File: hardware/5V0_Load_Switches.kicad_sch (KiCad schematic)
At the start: 28 parts, among them Q18 SI2302DDS-T1-GE3, Q19 SI2302DDS-T1-GE3, Q20 SI2302DDS-T1-GE3, U1 LMV321RIYLT, U10 INA199C3DCKR, U4 INA199C1DCKR, U5 NVTFS5116PLTAG, U6 NVTFS5116PLTAG, U7 NVTFS5116PLTAG, U9 INA199C3DCKR

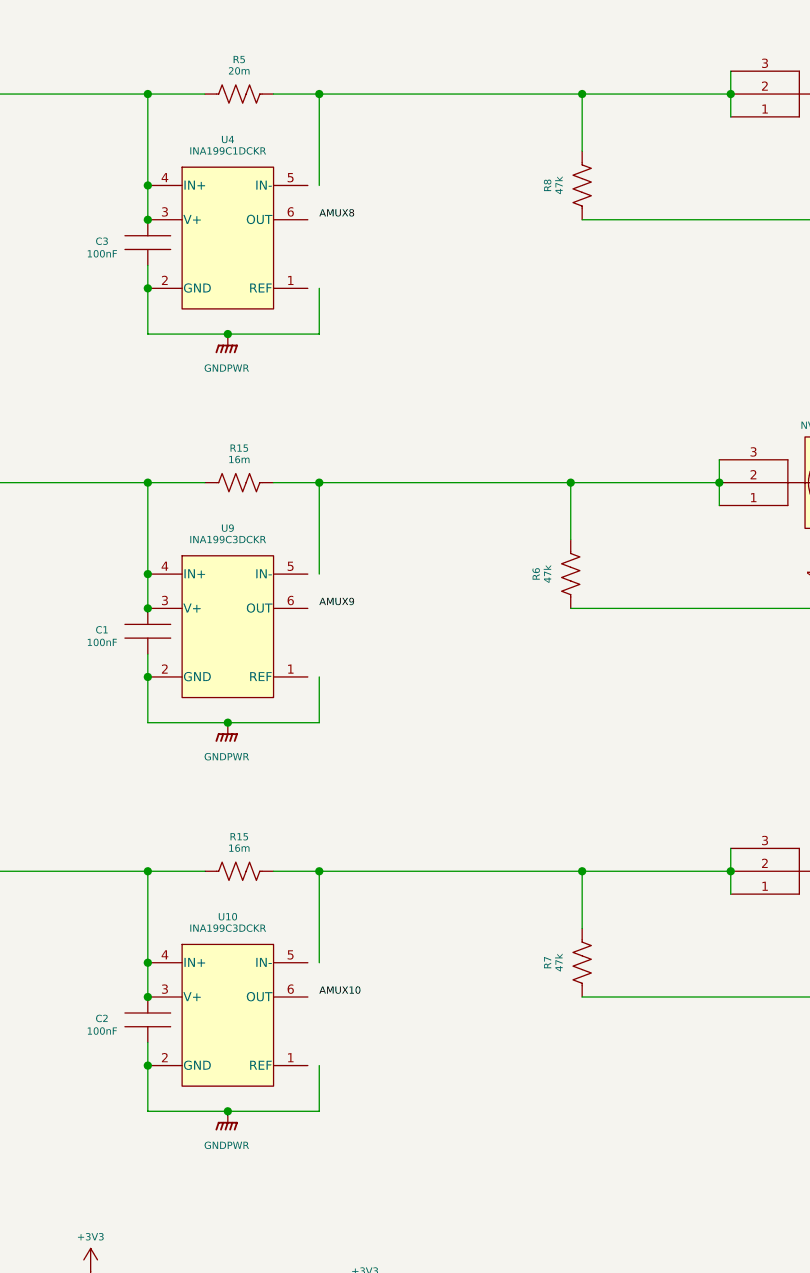
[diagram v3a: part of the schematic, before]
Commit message: hardware: Minor improvements to the schematics
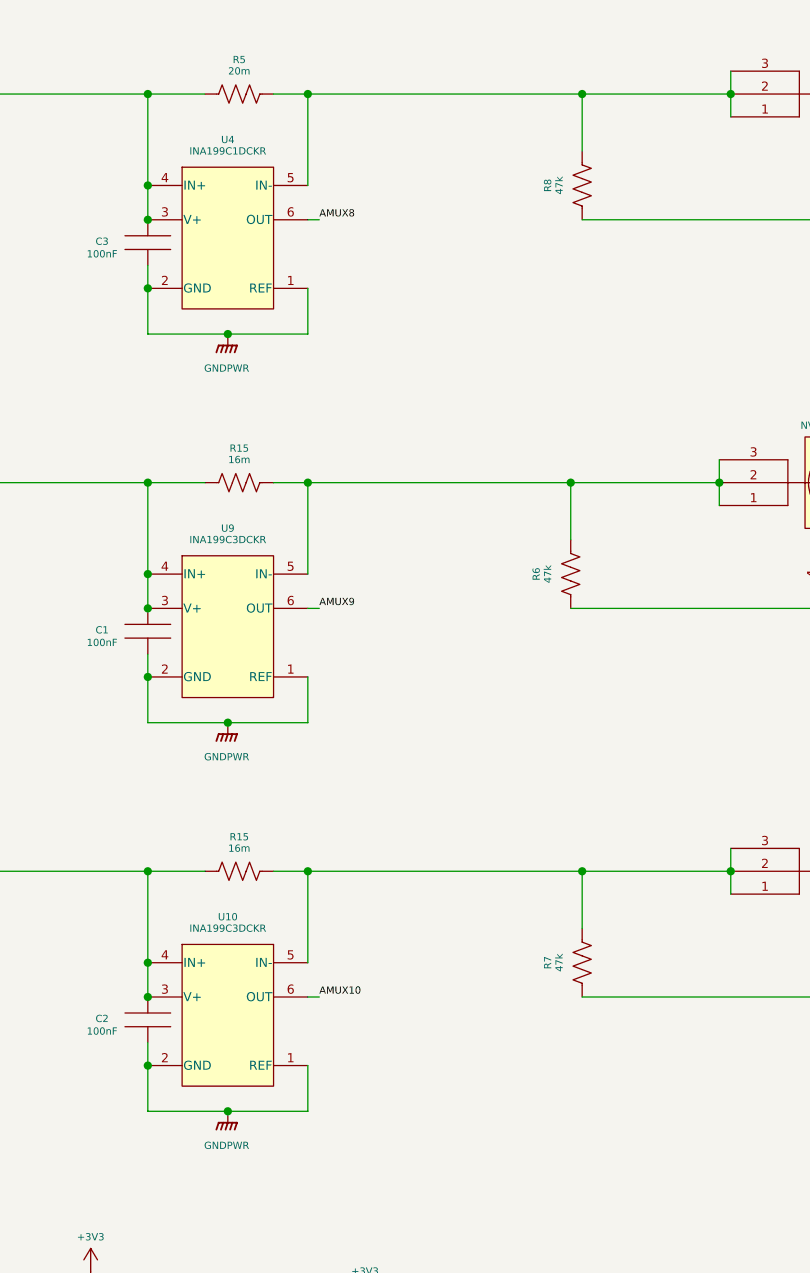
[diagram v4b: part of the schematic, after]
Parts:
- R106: MPN (none) -> CRCW060315K0FKEAHP; Manufacturer (none) -> Vishay; Package (none) -> SMD 0603; automotive Yes -> (none); automotive grade Grade 0 -> (none); category Res -> (none); composition Thick Film -> (none); device class L1 Passive Components -> (none); device class L2 Resistors -> (none); device class L3 Chip SMD Resistors -> (none); height 0.55mm -> (none); ipc land pattern name RESC16085X45 -> (none); lead free Yes -> (none); library id cdcefd0caca947c7 -> (none); manufacturer Vishay -> (none); package 0603 -> (none); power 250mW -> (none); power rating 0.33W -> (none); resistance 15kΩ -> (none); rohs Yes -> (none); series CRCW-HP e3 -> (none); temperature coefficient 100ppm/°C -> (none); temperature range high +155°C -> (none); temperature range low -55°C -> (none); tolerance 1% -> (none); voltage rating 75V -> (none)
- R2: symbol RC0805FR-0710KL:RES -> RC0805FR-0710KL:RC0805FR-0710KL; MPN (none) -> RC0805FR-0710KL; Manufacturer (none) -> YAGEO; Package (none) -> SMD 0805
- U4: footprint footprints:INA199C1DCKR -> footprints:INA199C1DCKR
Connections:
- net AMUX10: now also U10.6 (OUT)
- net AMUX8: now also U4.6 (OUT)
- net AMUX9: now also U9.6 (OUT)
- net GNDPWR: now also U10.1 (REF), U4.1 (REF), U9.1 (REF)
- net at R15.2, R7.2, U6.1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: now also U10.5 (IN-)
- net at R15.2, R6.2, U5.1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: now also U9.5 (IN-)
- net at R5.2, R8.2, U7.1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: now also U4.5 (IN-)

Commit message: hardware: Minor modifications for the upcoming release
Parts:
- R15: footprint footprints:WSL2010R0330FEA -> footprints:WSL2010R0160FEA; MPN WSL2010R0330FEA -> WSL2010R0160FEA
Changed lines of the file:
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@@
       (effects (font (size 0.8 0.8)))
     )
-    (property "Footprint" "footprints:WSL2010R0330FEA" (at 64.77 125.73 0)
+    (property "Footprint" "footprints:WSL2010R0160FEA" (at 64.77 125.73 0)
       (effects (font (size 1.27 1.27) italic) hide)
     )
@@
       (effects (font (size 1.27 1.27) italic) hide)
     )
-    (property "MPN" "WSL2010R0330FEA" (at 63.5 120.65 0)
+    (property "MPN" "WSL2010R0160FEA" (at 63.5 120.65 0)
       (effects (font (size 1.27 1.27)) hide)
     )
@@
       (effects (font (size 0.8 0.8)))
     )
-    (property "Footprint" "footprints:WSL2010R0330FEA" (at 64.77 82.55 0)
+    (property "Footprint" "footprints:WSL2010R0160FEA" (at 64.77 82.55 0)
       (effects (font (size 1.27 1.27) italic) hide)
     )
@@
       (effects (font (size 1.27 1.27) italic) hide)
     )
-    (property "MPN" "WSL2010R0330FEA" (at 63.5 77.47 0)
-      (effects (font (size 1.27 1.27)) hide)
-    )
+    (property "MPN" "WSL2010R0160FEA" (at 63.5 77.47 0)
+      (effects (font (size 1.27 1.27)) hide)
+    )

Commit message: hardware: update schematic and layout projects
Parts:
- R16: renamed from R2; Manufacturer YAGEO -> YAGEO
- U8: renamed from U4; Manufacturer TI -> Texas Instruments
- renumbered C3 to C4, C1 to C5, C2 to C6, C7 to C8, Q19 to Q21, Q18 to Q22, Q20 to Q23, R5 to R17, R15 to R18, R15 to R19, R6 to R20, R8 to R21, R7 to R22, R9 to R23, R11 to R24, R10 to R25, R12 to R26, R14 to R27, R13 to R28, U1 to U11, U5 to U12, U7 to U13, U6 to U14
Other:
- note removed: "ANALOG SIGNALS"
- note removed: "OUTPUTS CHARACTERISTICS"
- note removed: "POWER FLAGS"
- moved on the sheet: C4, C5, C6, C8, Q21, Q22, Q23, R106, R16, R17, R18, R19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
